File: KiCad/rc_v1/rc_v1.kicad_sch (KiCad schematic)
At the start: 36 parts, among them SW1 SLW-1276864-4A-D, SW10 TS12-66, SW11 TS12-1212, SW12 TS12-1212, SW3 TS12-66, SW4 TS12-66, SW5 TS12-66, SW6 TS12-66, SW7 TS12-66, SW8 TS12-66, SW9 TS12-66, U1 SDTx39xx2W, U2 SDTx39xx2W, U3 TM1637, U6 SN74LVC2G17DBVR

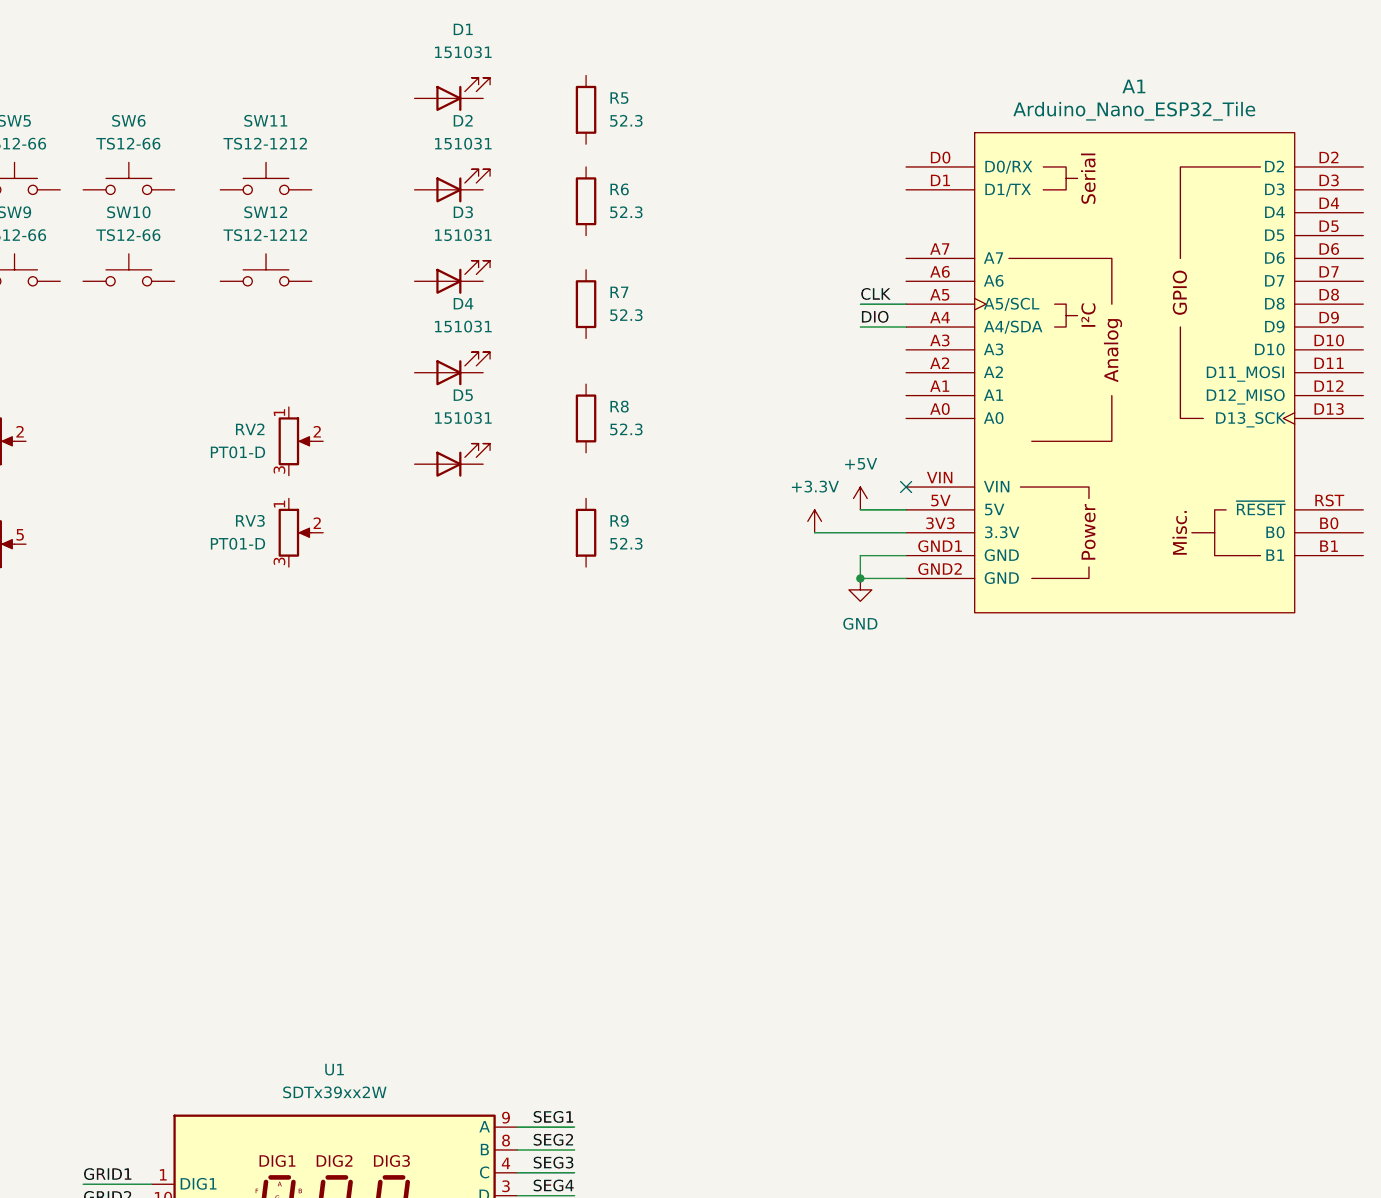
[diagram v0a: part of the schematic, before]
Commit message: Remote Controller PCB Milestone 2
Routed right side inputs
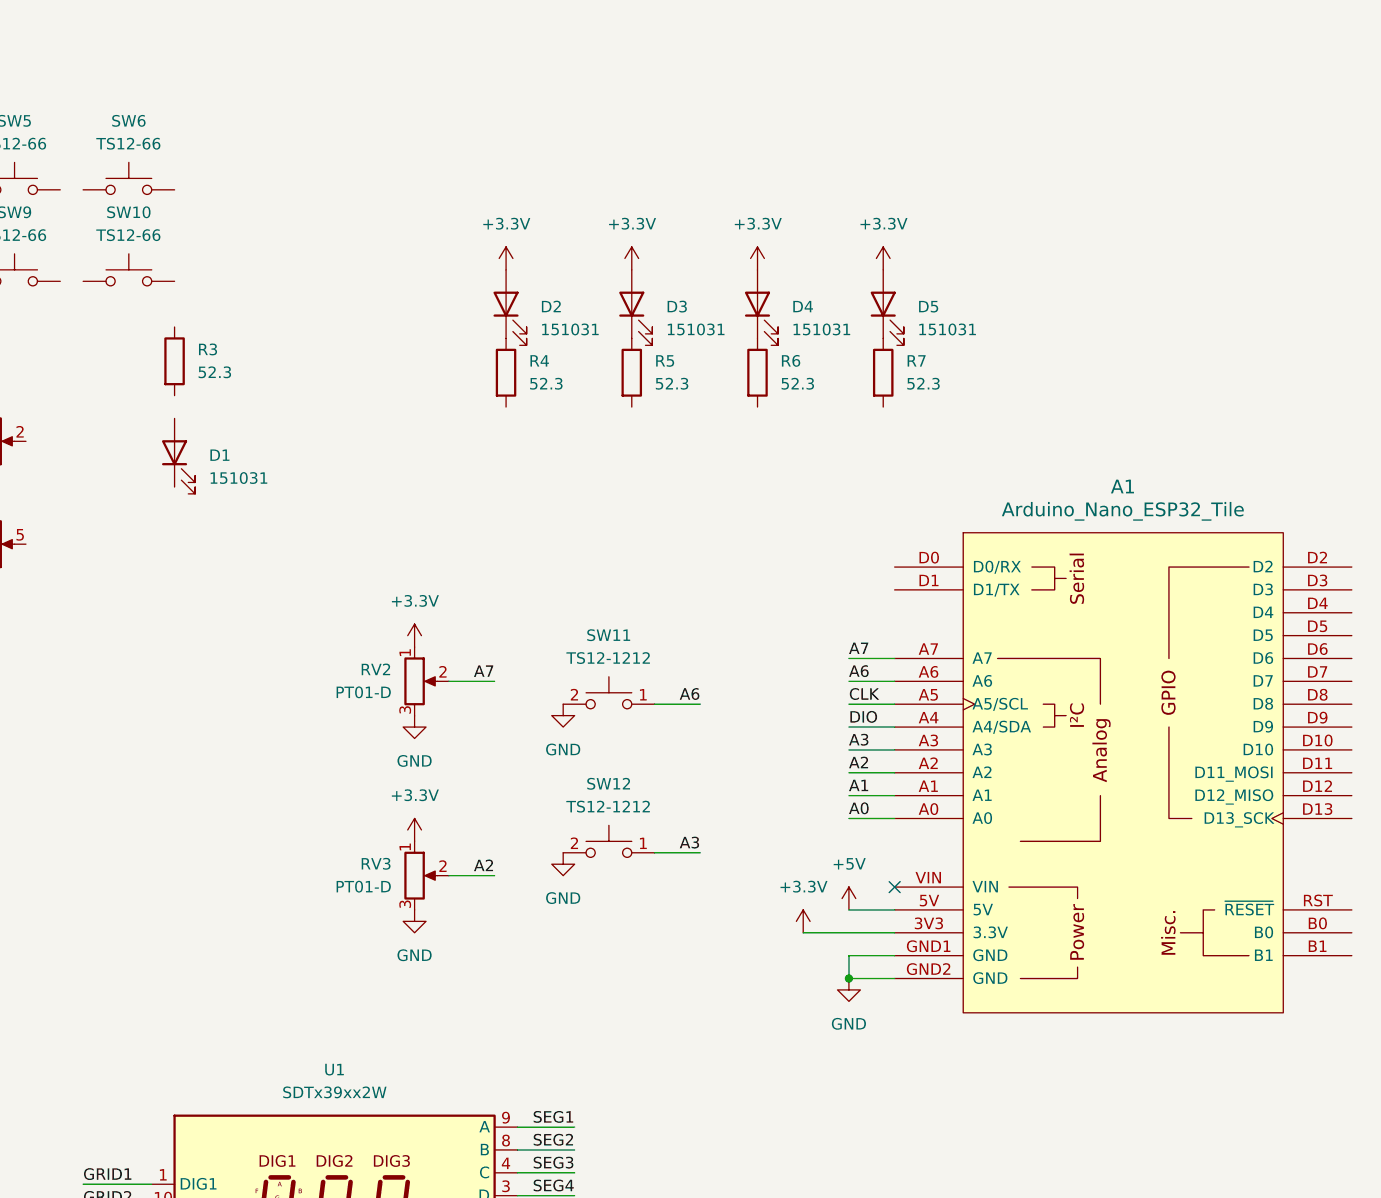
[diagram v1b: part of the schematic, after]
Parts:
- removed R8, R9: 52.3, Resistor_SMD:R_0805_2012Metric_Pad1.20x1.40mm_HandSolder, symbol Device:R
- added R3, R4: 52.3, Resistor_SMD:R_0805_2012Metric_Pad1.20x1.40mm_HandSolder, symbol Device:R
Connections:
- net +3.3V: now also D2.2 (A), D3.2 (A), D4.2 (A), D5.2 (A), RV2.1, RV3.1
- net GND: now also RV2.3, RV3.3, SW11.2, SW12.2
- net A0: now reaches A1.A0
- net A1: now reaches A1.A1
- net A2: now reaches A1.A2
- net A2: now also RV3.2
- net A3: now reaches A1.A3
- net A3: now also SW12.1
- net A6: now reaches A1.A6
- net A6: now also SW11.1
- net A7: now reaches A1.A7
- net A7: now also RV2.2
- net at D4.1 (K): now also R6.1
- net at D5.1 (K): now also R7.1
- net at D3.1 (K): now also R5.1
- net at D2.1 (K): now also R4.1
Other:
- moved on the sheet: A1, D1, D2, D3, D4, D5, R5, R6, RV2, RV3

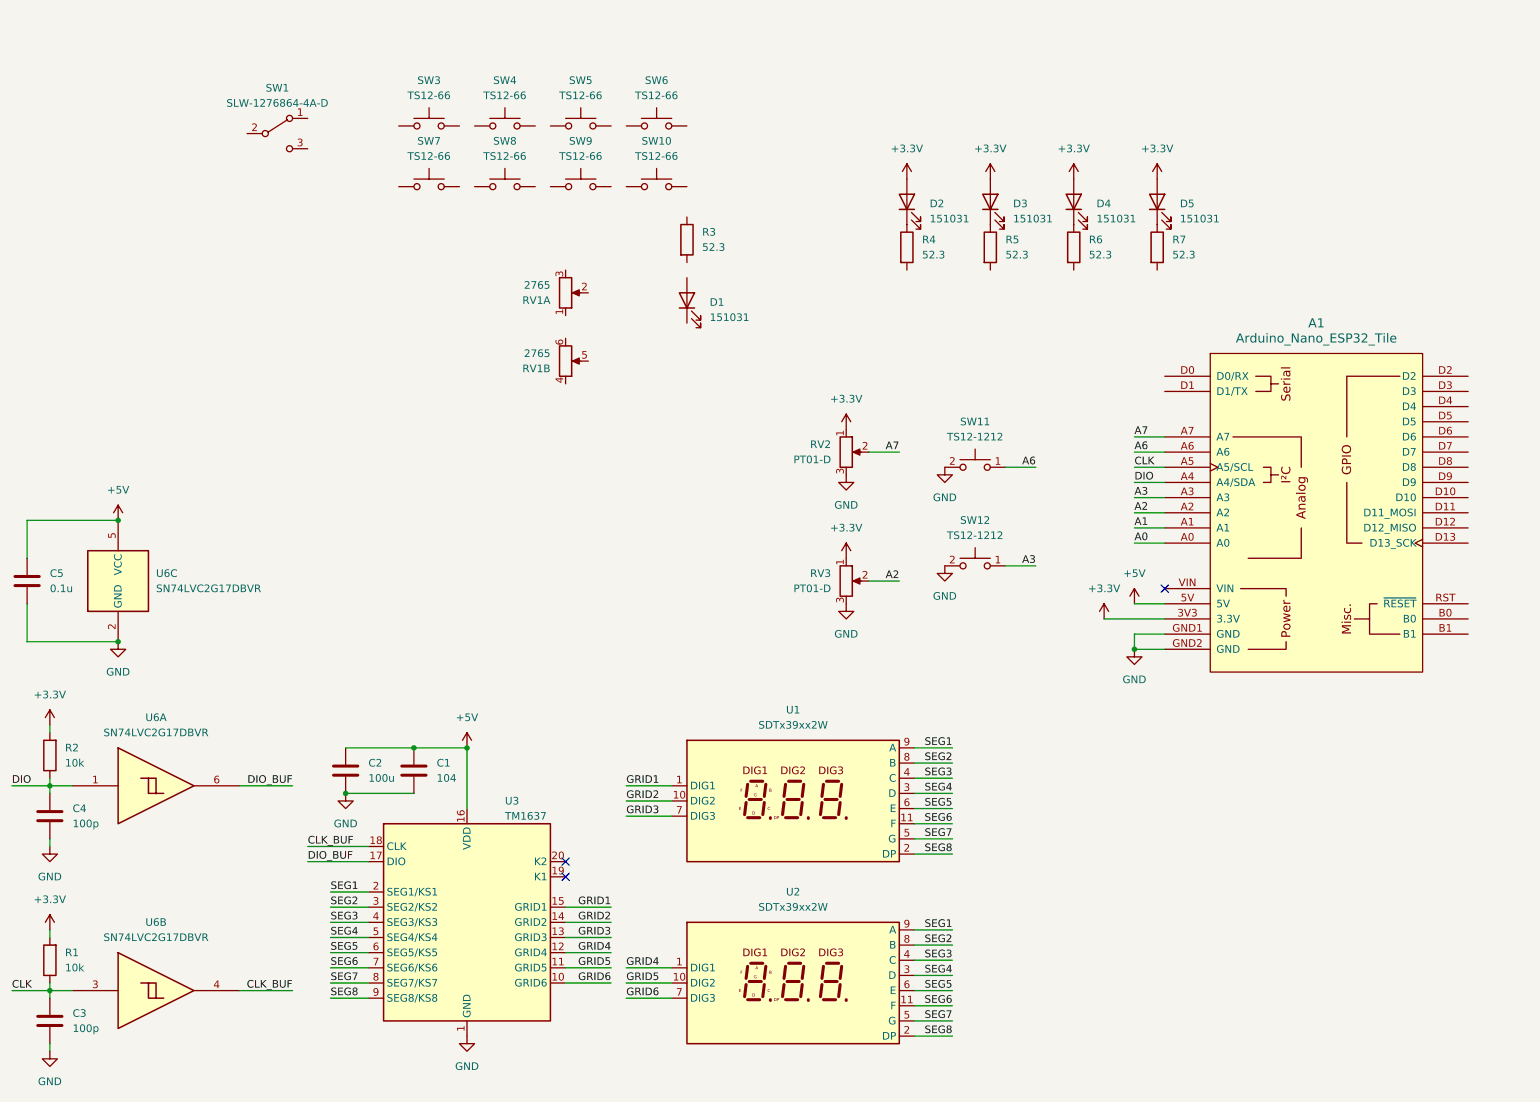
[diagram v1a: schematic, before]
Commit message: Remote Controller PCB Milestone 3
Tentatively completed all connections
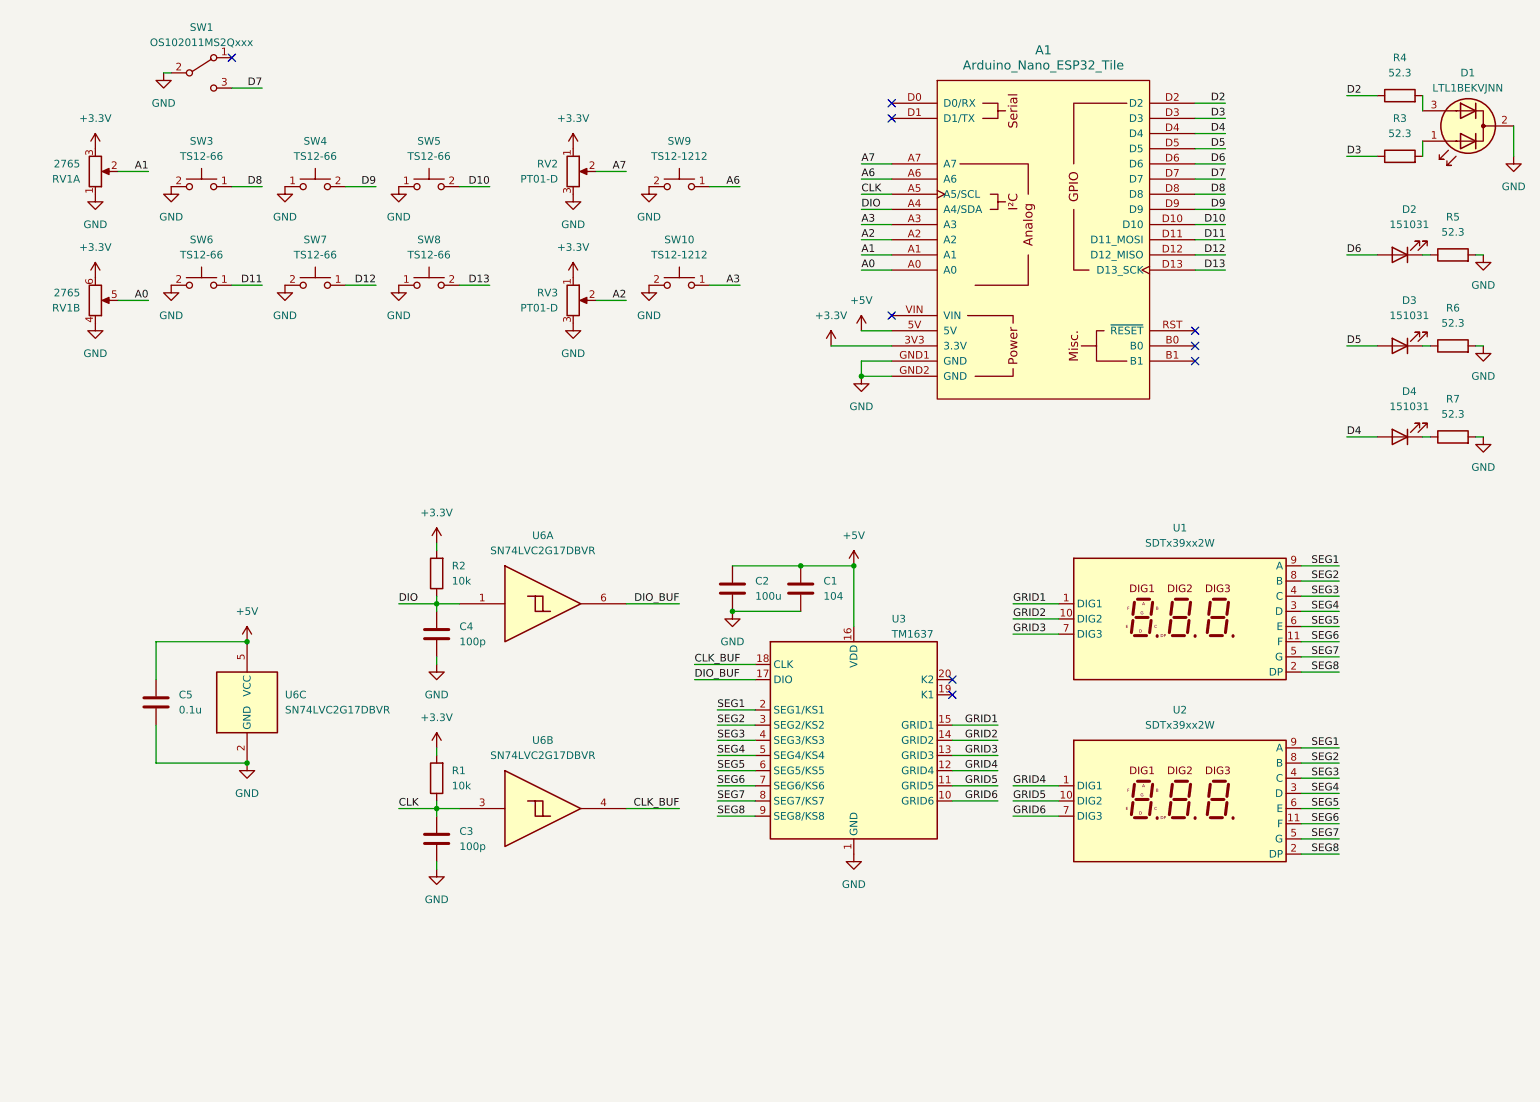
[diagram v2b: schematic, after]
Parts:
- removed D1, D5: 151031, LED_THT:LED_D3.0mm, symbol Device:LED
- removed SW10, SW9: TS12-66, Footprint Library:SW_PUSH_CUI_TS02-66-xxx-BK-xxx-xxx-D, symbol Switch:SW_Push
- added D1: LTL1BEKVJNN, LED_THT:LED_D3.0mm-3, symbol Device:LED_Dual_AKA
- SW1: value SLW-1276864-4A-D -> OS102011MS2Qxxx; footprint Footprint Library:SW_Slide_SPDT_CIT_SLW-1276864-4A-D -> Footprint Library:SW_Slide_SPDT_CK_OS102011MS2Qxxx
- renumbered SW12 to SW10, SW11 to SW9
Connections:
- net +3.3V: now also RV1.3, RV1.6; no longer D2.2 (A), D3.2 (A), D4.2 (A)
- net A0: now also RV1.5
- net A1: now also RV1.2
- net GND: now also R5.2, R6.2, R7.2, RV1.1, RV1.4, SW1.2 (B), SW3.2, SW4.1, SW5.1, SW6.2, SW7.2, SW8.1, D1.2 (K)
- net D10: now reaches SW5.2
- net D10: now also A1.D10
- net at D2.1 (K): now also R5.1; no longer R4.1
- net at R4.2: now also D1.3 (A2)
- net D9: now reaches SW4.2
- net D9: now also A1.D9
- net D11: now reaches A1.D11 (D11_MOSI)
- net D11: now also SW6.1
- net D12: now reaches A1.D12 (D12_MISO)
- net D12: now also SW7.1
- net D13: now reaches A1.D13 (D13_SCK)
- net D13: now also SW8.2
- net D2: now reaches A1.D2
- net D2: now also R4.1
- net D3: now reaches A1.D3
- net D3: now also R3.1
- net D4: now reaches A1.D4
- net D4: now also D4.2 (A)
- net D5: now reaches A1.D5
- net D5: now also D3.2 (A)
- net D6: now reaches A1.D6
- net D6: now also D2.2 (A)
- net D7: now reaches A1.D7
- net D7: now also SW1.3 (C)
- net D8: now reaches A1.D8
- net D8: now also SW3.1
- net at R3.2: now also D1.1 (A1)
- net at D4.1 (K): now also R7.1; no longer R6.1
- net at D3.1 (K): now also R6.1; no longer R5.1
- no-connect marks 3 -> 9
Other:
- moved on the sheet: A1, C1, C2, C3, C4, C5, D2, D3, D4, R1, R2, R3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
